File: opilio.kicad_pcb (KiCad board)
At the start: 4 copper layers, 80 x 40 mm, 89 parts, among them J1 Screw_Terminal_01x02, J2 USB_B_Micro, J3 Conn_01x02_Male, J4 Conn_01x02_Male, J5 Conn_01x02_Male, Q1 PMV25ENEAR, U1 EUP3458, U2 STM32F103C8T6, Y1 YSX531SL 8MHz, Y2 YST310S 32.768KHz

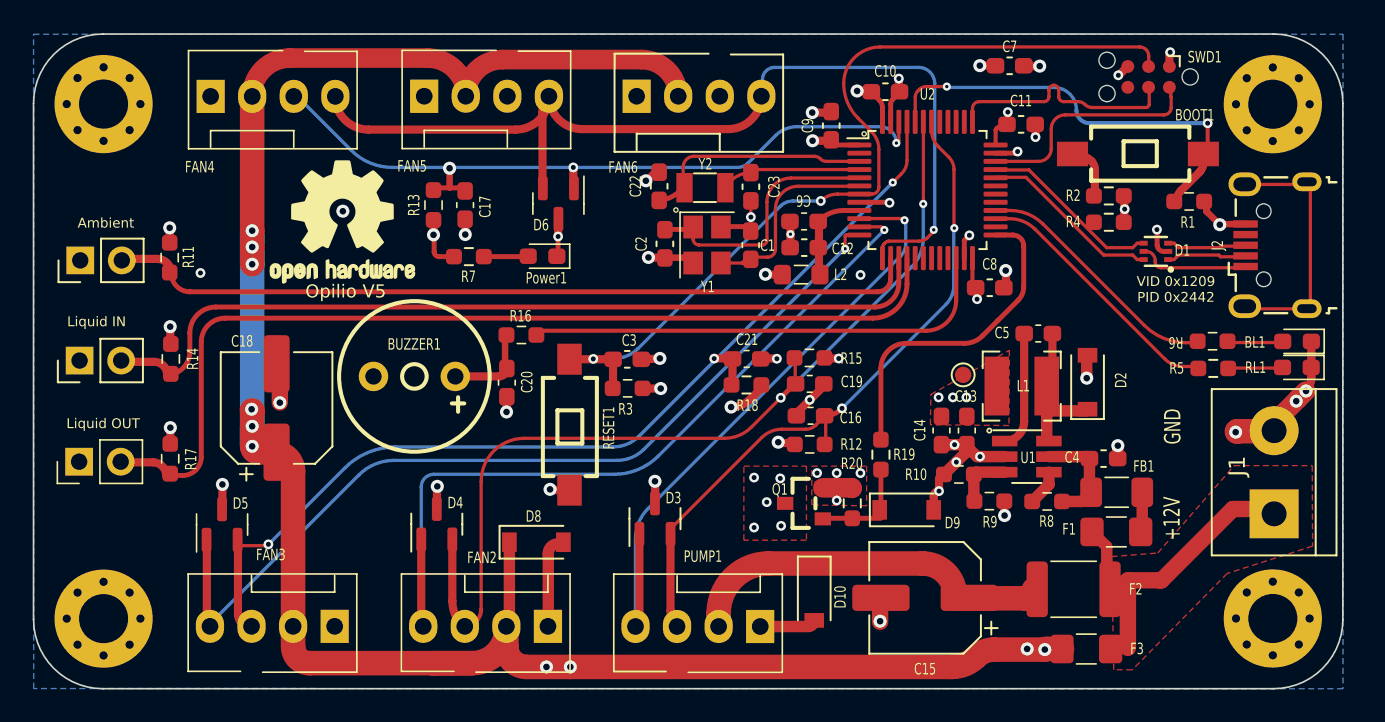
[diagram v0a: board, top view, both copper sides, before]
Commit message: bigger pads for mosfets
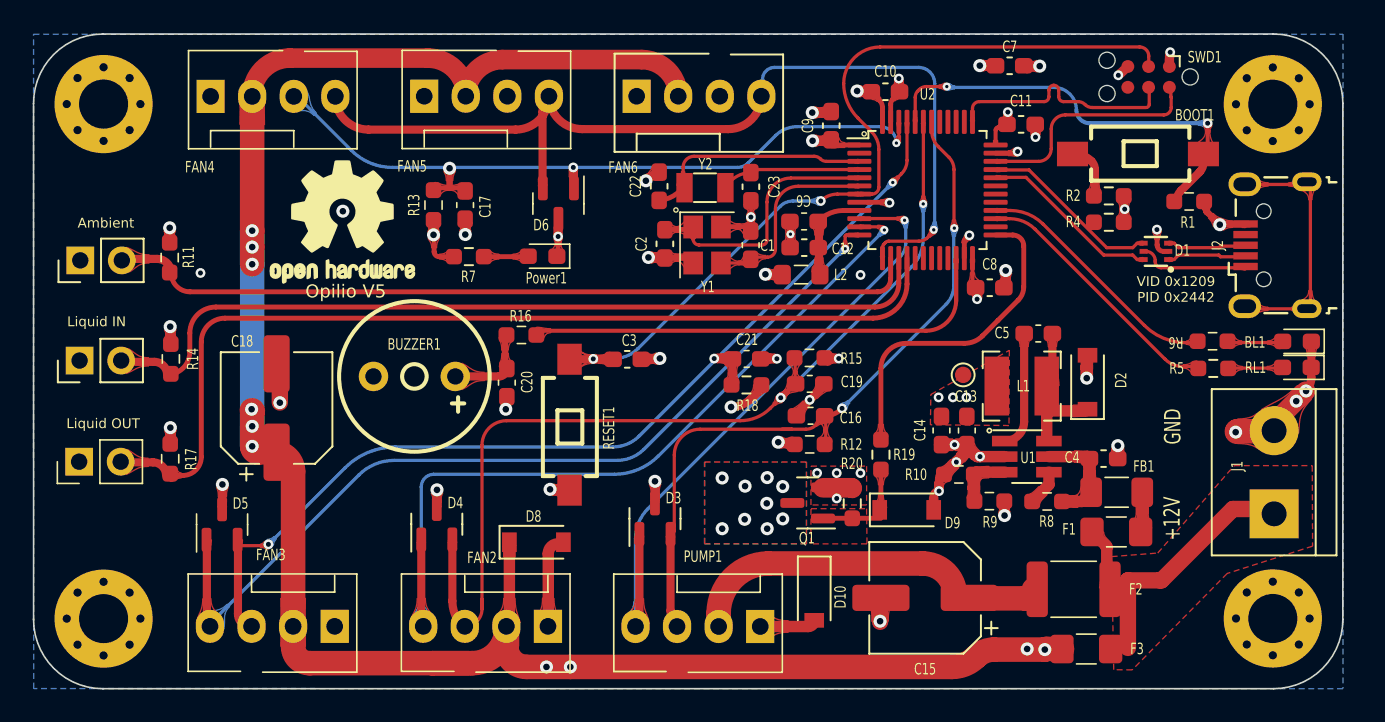
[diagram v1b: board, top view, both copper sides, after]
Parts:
- removed R3: 10k, Resistor_SMD:R_0603_1608Metric_Pad0.98x0.95mm_HandSolder
- C3: value 100nF -> 10nF
- Q1: footprint easyeda2kicad:SOT-23_L2.9-W1.3-P1.90-LS2.4-BR -> Package_TO_SOT_SMD:SOT-23
- moved Q1 0.23 mm to (147.3, 128.7), turned to 180 degrees
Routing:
- net PWM_READ1: track 41.0 -> 45.0 mm
- net NRST: track 56.0 -> 54.2 mm
- net PWM_READ2: track 58.1 -> 59.7 mm
- net +3.3V: track 26.9 -> 25.8 mm, vias 20 -> 19
- net D: vias 5 -> 9
- added copper zone on B.Cu, net D
- added copper zone on F.Cu, net Net-(D9-Pad1)

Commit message: added 3d models
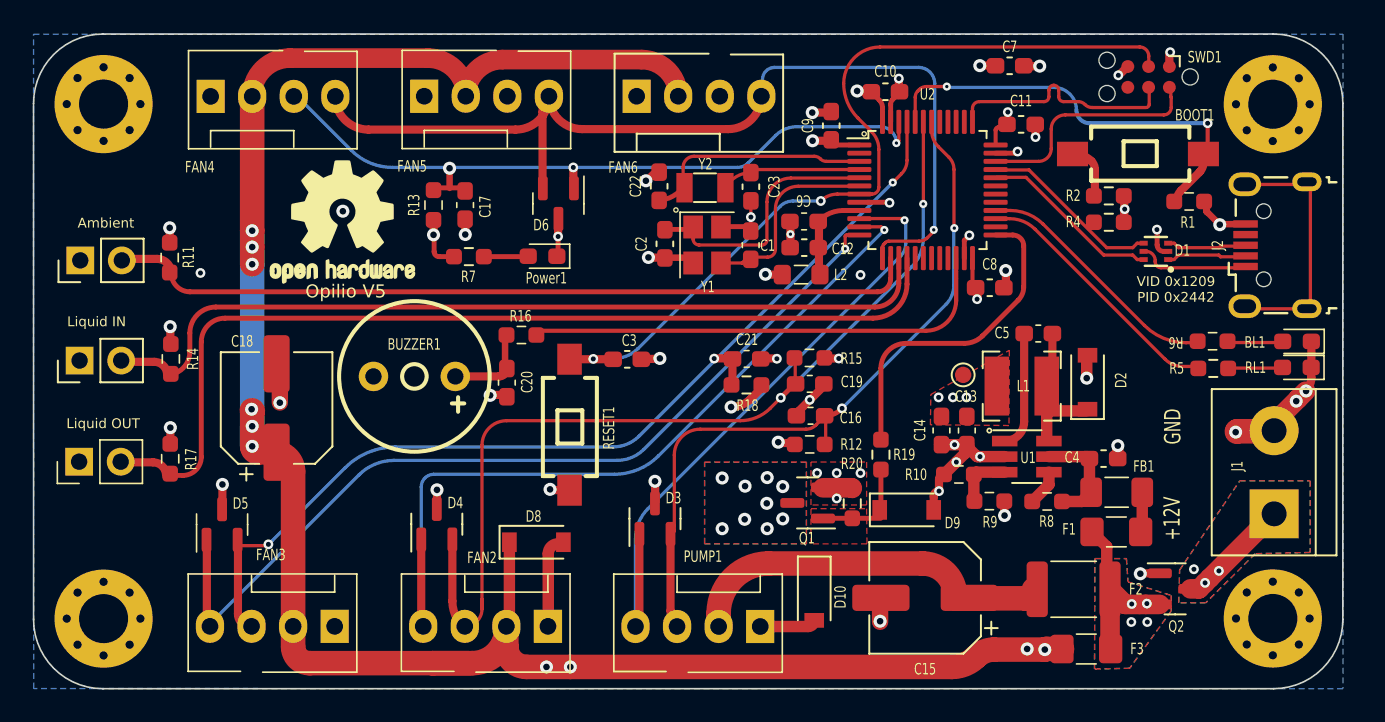
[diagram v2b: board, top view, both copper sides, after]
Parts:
- added Q2: AO3401A, Package_TO_SOT_SMD:SOT-23, F.Cu at (169.8, 133.9)
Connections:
- F1 pad 1: +12V -> 12vP
- F2 pad 2: +12V -> 12vP
- F3 pad 2: +12V -> 12vP
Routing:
- net +12V: track 18.6 -> 7.01 mm, vias 0 -> 3
- net 12vP: track 0.00 -> 10.9 mm, vias 0 -> 4
- net GND: track 62.9 -> 63.8 mm, vias 43 -> 44
- net PWM_READ1: track 45.0 -> 44.4 mm
- net COUT: track 8.61 -> 8.03 mm
- added copper zone on B.Cu, net +12V
- added copper zone on B.Cu, net 12vP
- added copper zone on F.Cu, net 12vP

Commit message: cleanup and annotate schema
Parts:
- D1: footprint easyeda2kicad:SOT-666-6_L1.6-W1.2-P0.50-LS1.6-BL -> Package_TO_SOT_SMD:SOT-666
- F2: value 3A -> 2A; footprint Fuse:Fuse_1812_4532Metric_Pad1.30x3.40mm_HandSolder -> Fuse:Fuse_1206_3216Metric_Pad1.42x1.75mm_HandSolder
- R20: value 10K -> 7k5
- moved R1 17.7 mm to (155.0, 101.9), turned to 180 degrees
- moved R4 3.62 mm to (169.3, 111.1), turned to 0 degrees
- moved R2 3.61 mm to (169.3, 109.6), turned to 0 degrees
- moved F2 0.95 mm to (164.3, 134.5)
- moved BOOT1 0.31 mm to (167.5, 107.0), turned to 0 degrees
- moved D1 0.22 mm to (168.8, 113.3), turned to 180 degrees
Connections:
- R4 pad 2: USB_D+ -> USB_CON_D+
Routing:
- net BOOT0: track 25.9 -> 16.9 mm
- net USB_D-: track 11.1 -> 13.3 mm
- net USB_D+: track 11.1 -> 13.0 mm
- net USB_CON_D+: track 4.49 -> 6.21 mm
- net +12VF(P): track 26.3 -> 27.8 mm
- net +5V: track 6.80 -> 7.54 mm
- net +3.3V: track 25.8 -> 26.3 mm

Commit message: copper pour
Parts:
- moved C9 0.14 mm to (148.6, 105.6)
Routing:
- net +3.3V: track 26.3 -> 23.9 mm
- net GND: vias 44 -> 51

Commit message: WIP:0402
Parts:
- C1, C10, C11, C16, C17, C19, C2, C20, C21, C22, C23, C3, C6, C8, C9: footprint Capacitor_SMD:C_0603_1608Metric_Pad1.08x0.95mm_HandSolder -> Capacitor_SMD:C_0402_1005Metric_Pad0.74x0.62mm_HandSolder
- R1, R10, R11, R12, R13, R14, R15, R16, R17, R18, R2, R20, R4, R5, R6, R7, R8, R9: footprint Resistor_SMD:R_0603_1608Metric_Pad0.98x0.95mm_HandSolder -> Resistor_SMD:R_0402_1005Metric_Pad0.72x0.64mm_HandSolder
- moved R18 3.66 mm to (139.9, 121.0), turned to 0 degrees
- moved C21 3.65 mm to (139.9, 120.0), turned to 0 degrees
- moved R8 0.41 mm to (162.3, 128.4)
- moved R4 0.41 mm to (169.6, 110.8)
- moved R9 0.40 mm to (158.1, 128.3)
- moved C3 0.38 mm to (135.9, 119.9)
- moved R16 0.36 mm to (129.5, 118.5)
- moved R2 0.30 mm to (169.6, 109.7)
- moved C17 0.28 mm to (126.4, 110.2)
- moved R13 0.23 mm to (124.4, 110.2)
- moved C9 0.21 mm to (148.7, 105.8)
- moved C10 0.19 mm to (152.2, 103.6)
- moved C23 0.19 mm to (143.7, 109.4)
- moved C1 0.17 mm to (143.7, 112.9)
- moved C22 0.17 mm to (138.3, 109.5)
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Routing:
- net +3.3V: track 23.9 -> 21.8 mm
- net GND: track 64.2 -> 65.5 mm
- net BUZZER: track 30.9 -> 31.9 mm
- net Net-(C4-Pad1): track 6.32 -> 5.53 mm
- net BLUE_LED: track 15.1 -> 15.8 mm
- net PWM_READ3: track 61.4 -> 60.8 mm
- net RED_LED: track 15.8 -> 16.3 mm

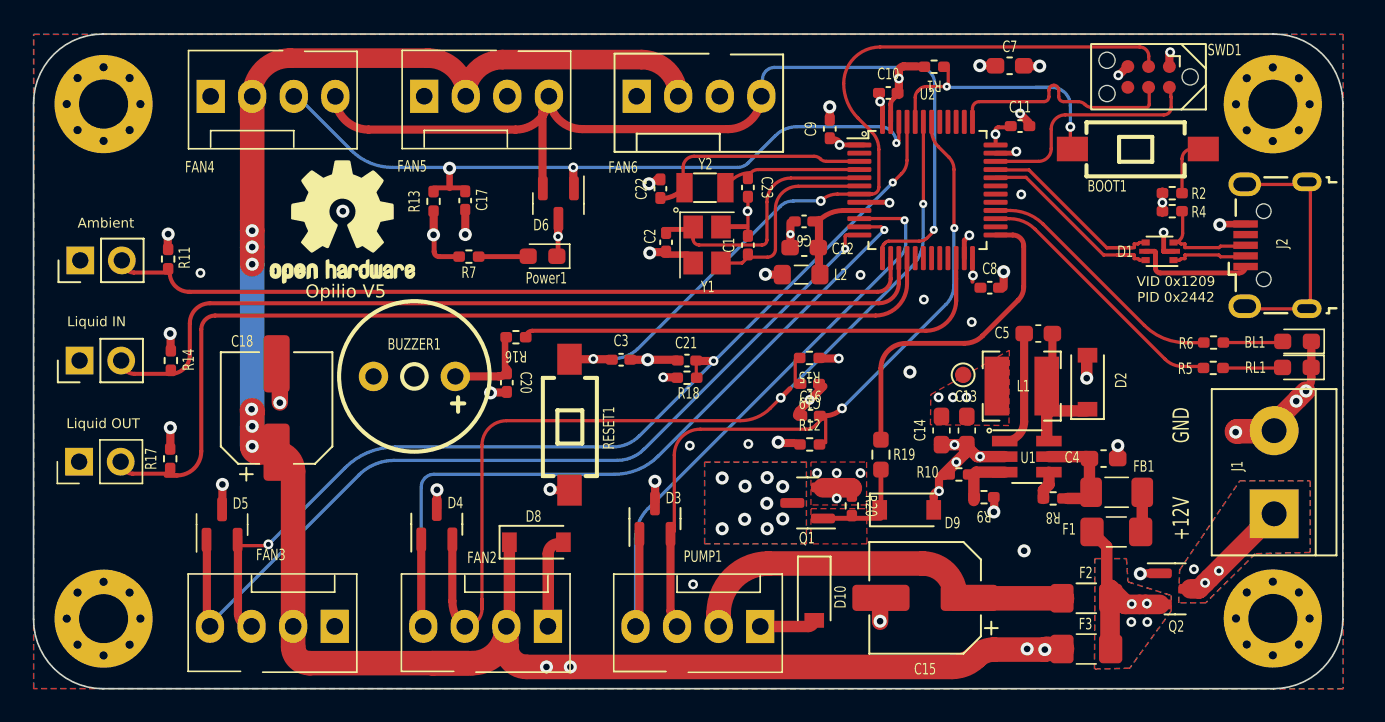
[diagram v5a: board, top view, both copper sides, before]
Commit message: shrink board, 0402 passives
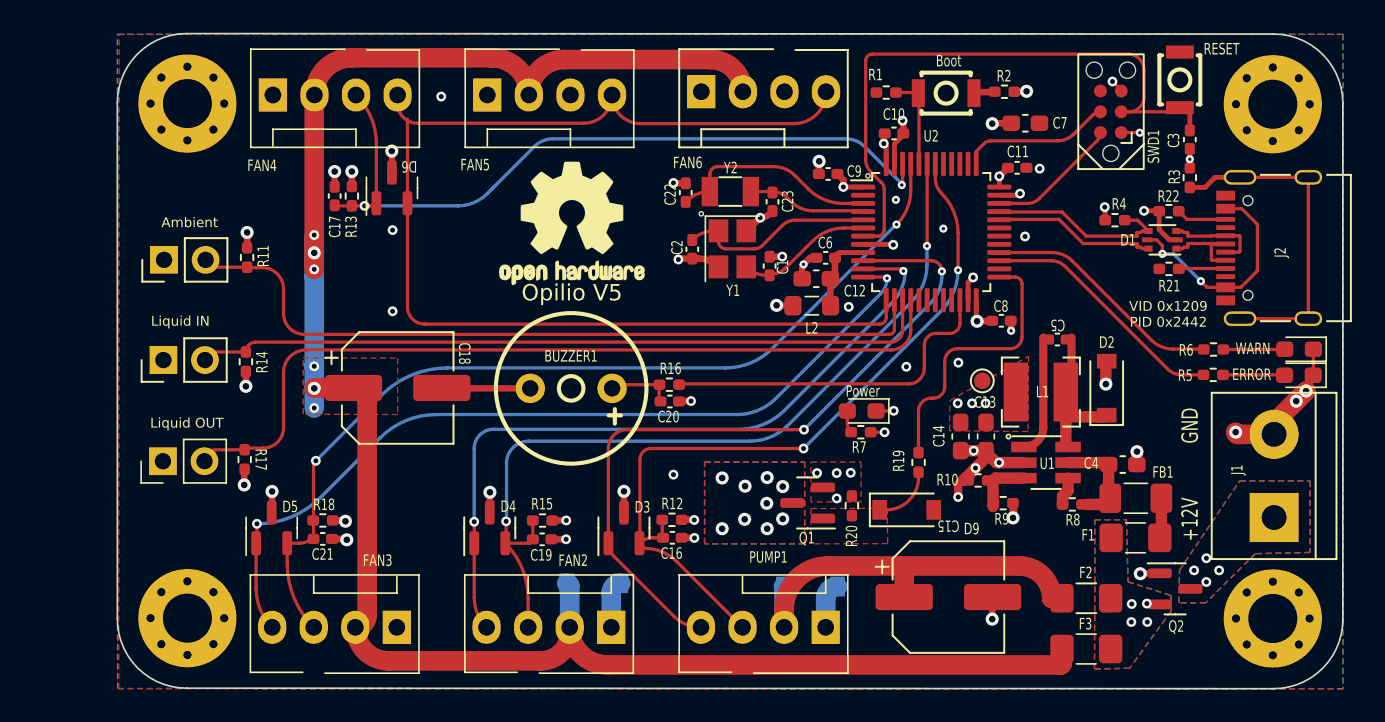
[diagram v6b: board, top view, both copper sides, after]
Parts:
- removed BOOT1: Boot, easyeda2kicad:SW-SMD_L6.0-W3.3-LS8.0
- removed RESET1: Reset, easyeda2kicad:SW-SMD_L6.0-W3.3-LS8.0
- added R21: 5K11, Resistor_SMD:R_0402_1005Metric_Pad0.72x0.64mm_HandSolder, F.Cu at (169.4, 114.3)
- added R22: 5K11, Resistor_SMD:R_0402_1005Metric_Pad0.72x0.64mm_HandSolder, F.Cu at (169.4, 110.8)
- added R3: 1M, Resistor_SMD:R_0402_1005Metric_Pad0.72x0.64mm_HandSolder, F.Cu at (170.7, 108.8)
- added SW1: Reset, easyeda2kicad:SW-SMD_L3.0-W2.5-P3.40-LS4.0-L, F.Cu at (170.0, 102.8)
- added SW2: Boot, easyeda2kicad:SW-SMD_L3.0-W2.5-P3.40-LS4.0-L, F.Cu at (155.8, 103.6)
- C5: footprint Capacitor_SMD:C_0603_1608Metric_Pad1.08x0.95mm_HandSolder -> Capacitor_SMD:C_0402_1005Metric_Pad0.74x0.62mm_HandSolder
- D10, D8: moved to B.Cu
- J2: value USB_B_Micro -> USB_C_Receptacle_USB2.0; footprint Custom:USB_Micro-B_Wuerth_629105150521_narrow_holes -> Custom:USB_C_Receptacle_Palconn_UTC16-G_Streached_pads
- R1: value 100k -> 100K
- R10: value 24k -> 24K
- R11, R14, R17: value 10k -> 10K
- R19: footprint Resistor_SMD:R_0603_1608Metric_Pad0.98x0.95mm_HandSolder -> Resistor_SMD:R_0402_1005Metric_Pad0.72x0.64mm_HandSolder
- R20: value 7k5 -> 7K5
- R4: value 1k5 -> 1K5
- R5: value 165R -> 200R
- R6: value R660 -> 680R
- R7: value 1.65K -> 2K
- R9: value 75k -> 75K
- moved C3 37.3 mm to (170.7, 106.5), turned to -90 degrees
- moved R7 26.2 mm to (150.6, 124.3), turned to 180 degrees
- moved C21 24.8 mm to (117.7, 130.8), turned to 180 degrees
- moved R18 23.9 mm to (117.7, 129.7), turned to 180 degrees
- moved Power1 21.7 mm to (150.6, 123.0)
- moved R15 19.1 mm to (131.1, 129.7)
- moved C19 18.9 mm to (131.1, 130.9)
- moved LOGO1 14.0 mm to (132.9, 111.6)
- moved R2 12.0 mm to (159.3, 103.5), turned to 180 degrees
- moved C16 11.3 mm to (139.0, 130.8), turned to 180 degrees
- moved D6 10.2 mm to (121.9, 109.4), turned to 90 degrees
- moved C20 10.0 mm to (138.9, 122.5), turned to 0 degrees
- moved R16 9.81 mm to (138.8, 121.4)
- moved BUZZER1 9.61 mm to (132.8, 121.7)
- moved R12 9.59 mm to (139.0, 129.7), turned to 180 degrees
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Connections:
- D1 pad 1: USB_CON_D- -> USBC_D-
- D1 pad 3: USB_CON_D+ -> USBC_D+
- R4 pad 2: USB_CON_D+ -> USB_D+
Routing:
- net +12VF(F): track 187.7 -> 120.0 mm, vias 10 -> 6
- net Net-(J2-PadS1): track 0.00 -> 20.3 mm
- net NRST: track 54.2 -> 38.0 mm, vias 2 -> 0
- net unconnected-(J2-Pad6): track 14.6 -> 0.00 mm
- net BOOT0: track 16.9 -> 5.59 mm, vias 2 -> 0
- net 12vP: track 10.9 -> 0.00 mm
- net BUZZER: track 31.9 -> 21.2 mm
- net PWM_OUT4: track 61.7 -> 72.3 mm, vias 1 -> 0
- net WATER_OUT_T: track 60.0 -> 50.7 mm
- net PWM_READ2: track 59.7 -> 50.8 mm
- net WATER_IN_T: track 53.3 -> 44.7 mm
- net GND: track 65.5 -> 58.3 mm, vias 51 -> 50
- net +12V: track 7.01 -> 0.00 mm, vias 3 -> 4
- net SWIO: track 14.5 -> 8.06 mm
- net +5V: track 7.54 -> 13.8 mm, vias 0 -> 2
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- added copper zone on F.Cu, net +12VF(F)
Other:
- board size 80 x 40 mm -> 74.9 x 40 mm

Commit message: built
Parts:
- D10, D8: footprint Diode_SMD:D_SOD-123 -> Diode_SMD:D_SMA-SMB_Universal_Handsoldering
- moved D10 1.03 mm to (147.4, 132.7)
- moved D8 0.86 mm to (134.3, 132.7)
- moved C5 0.29 mm to (162.5, 119.0)
- moved SW1 0.27 mm to (170.3, 102.8)
- moved R8 0.15 mm to (163.4, 128.6)
- moved R1 0.14 mm to (152.2, 103.6)
- moved R9 0.09 mm to (159.2, 128.6)
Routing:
- net Net-(J2-PadS1): track 20.3 -> 29.9 mm
- net GND: track 58.3 -> 63.9 mm, vias 50 -> 53
- net D: track 5.87 -> 11.1 mm
- net Net-(D9-Pad1): track 3.43 -> 7.11 mm
- net +12VF(P): track 25.1 -> 26.7 mm
- net +5V: track 13.8 -> 12.3 mm, vias 2 -> 3
- net +12VF(F): track 120.0 -> 121.3 mm
